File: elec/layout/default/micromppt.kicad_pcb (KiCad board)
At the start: 2 copper layers, 25.9 x 15.3 mm, 16 parts

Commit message: fixed :woozy:
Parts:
- C5: value 1nF ±10% 50V X7R -> 1nF ±20% 50V X7R
- R6: footprint lib:R1206 -> atopile:R1206-bdb864
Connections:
- C1 pad 1: hv-1 -> hv
- C3 pad 1: hv -> hv-1
- R1 pad 1: hv -> hv-1
- R2 pad 1: p3 -> net
- R3 pad 1: hv-1 -> hv
- R5 pad 2: hv -> hv-1
- R6 pad 2: hv -> hv-1
- U2 pad 1: net -> VR2-net
- U2 pad 3: p3 -> net
- U3 pad 1: hv-1 -> hv
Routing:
- net hv-1: track 8.72 -> 13.9 mm, vias 1 -> 3
- net hv: track 13.9 -> 8.72 mm, vias 3 -> 1
- net p3: track 2.22 -> 0.00 mm
- net net: track 0.00 -> 2.22 mm

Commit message: fixed
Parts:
- added U5: , lib:SOD-80_L3.5-W1.5-RD, F.Cu at (50.0, -5.00)
- added U6: 10kΩ ±1% 62.5mW, atopile:R0402-56259e, F.Cu at (10.0, -5.00)
- U2: footprint lib:RES-ADJ-SMD_3224W -> lib:SOT-23_L2.9-W1.3-P1.90-LS2.4-BR
- moved U2 59.4 mm to (80.0, -5.00)
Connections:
- net cathode renamed VOUT
- C1 pad 1: hv -> S
- C3 pad 1: hv-1 -> hv
- R1 pad 1: hv-1 -> hv
- R2 pad 1: net -> VCTRL
- R3 pad 1: hv -> S
- R5 pad 2: hv-1 -> hv
- R6 pad 2: hv-1 -> hv
- U2 pad 1: VR2-net -> G
- U2 pad 2: VCTRL -> S
- U2 pad 3: net -> D
- U3 pad 1: hv -> S
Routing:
- net (no net): track 0.00 -> 21.7 mm, vias 0 -> 3
- net hv-1: track 13.9 -> 0.00 mm, vias 3 -> 0
- net VCTRL: track 13.0 -> 0.00 mm, vias 2 -> 0
- net hv: track 8.72 -> 13.9 mm, vias 1 -> 3
- added copper zone on F.Cu, net (none)
- removed copper zone on F.Cu, net hv-1

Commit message: Micromppt V3 (fr this time)
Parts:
- removed C1: 10µF ±10% 10V X5R, atopile:C0603-bd72f6
- added D1: , lib:SOD-323F_L1.7-W1.3-LS2.5-R-RD, F.Cu at (67.7, 51.9)
- added U7: , lib:CONN-SMD_2P-P2.50_DEALON_XH-2PS, F.Cu at (86.8, 56.3)
- added U8: , lib:CONN-SMD_2P-P2.50_DEALON_XH-2PS, F.Cu at (74.8, 56.3)
- U5: value (none) -> 10µF ±10% 10V X5R; footprint lib:SOD-80_L3.5-W1.5-RD -> atopile:C0603-bd72f6
- moved U6 78.5 mm to (67.6, 48.4), turned to 90 degrees
- moved U2 57.6 mm to (70.7, 51.8), turned to 180 degrees
- moved U5 52.9 mm to (67.6, 44.9), turned to -90 degrees
- moved R2 4.85 mm to (79.0, 52.2), turned to 180 degrees
- moved R3 3.49 mm to (77.0, 44.3)
- moved C3 3.09 mm to (86.5, 50.0), turned to 0 degrees
- moved U3 1.05 mm to (72.0, 46.7)
- moved C4 0.76 mm to (86.7, 44.1)
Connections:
- net S renamed C
- U2 pad 1: G -> A
- U4 pad 1: gnd -> (no net)
- U4 pad 2: gnd -> (no net)
- U4 pad 3: gnd -> (no net)
- U5 pad 2: G -> gnd
- U6 pad 1: G -> A
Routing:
- net C: track 0.00 -> 21.8 mm
- net (no net): track 21.7 -> 0.00 mm, vias 3 -> 0
- net VCTRL: track 0.00 -> 11.5 mm, vias 0 -> 2
- net hv: track 13.9 -> 20.4 mm, vias 3 -> 2
- net D: track 0.00 -> 4.27 mm
- net A: track 0.00 -> 3.85 mm
- net VOUT: track 15.4 -> 12.7 mm
- net net: track 2.22 -> 0.00 mm
- net gnd: track 4.64 -> 2.81 mm, vias 23 -> 10
- net XSHUT: track 16.7 -> 15.5 mm
- added copper zone on F.Cu, net C
- removed copper zone on F.Cu, net hv
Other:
- board size 25.9 x 15.3 mm -> 25.9 x 17.7 mm

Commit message: Micromppt V3 (fr this time) x2
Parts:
- moved R2 0.53 mm to (79.5, 52.5)
- moved D1 0.50 mm to (67.4, 52.3)
- moved U8 0.40 mm to (74.5, 56.3)
- moved U2 0.35 mm to (70.3, 51.9)
- moved R1 0.26 mm to (82.9, 52.5)
- moved U7 0.11 mm to (86.8, 56.3)
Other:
- board size 25.9 x 17.7 mm -> 25.7 x 17.5 mm

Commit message: Micromppt V3 added githash
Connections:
- net VOUT renamed cathode
- U4 pad 1: (no net) -> gnd
- U4 pad 2: (no net) -> gnd
- U4 pad 3: (no net) -> gnd
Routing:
- net gnd: track 2.81 -> 6.24 mm, vias 10 -> 16
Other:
- board text added: "+"
- board text added: "BAT"
- board text added: "PV"
- board text added: "{{GITHASH}}"

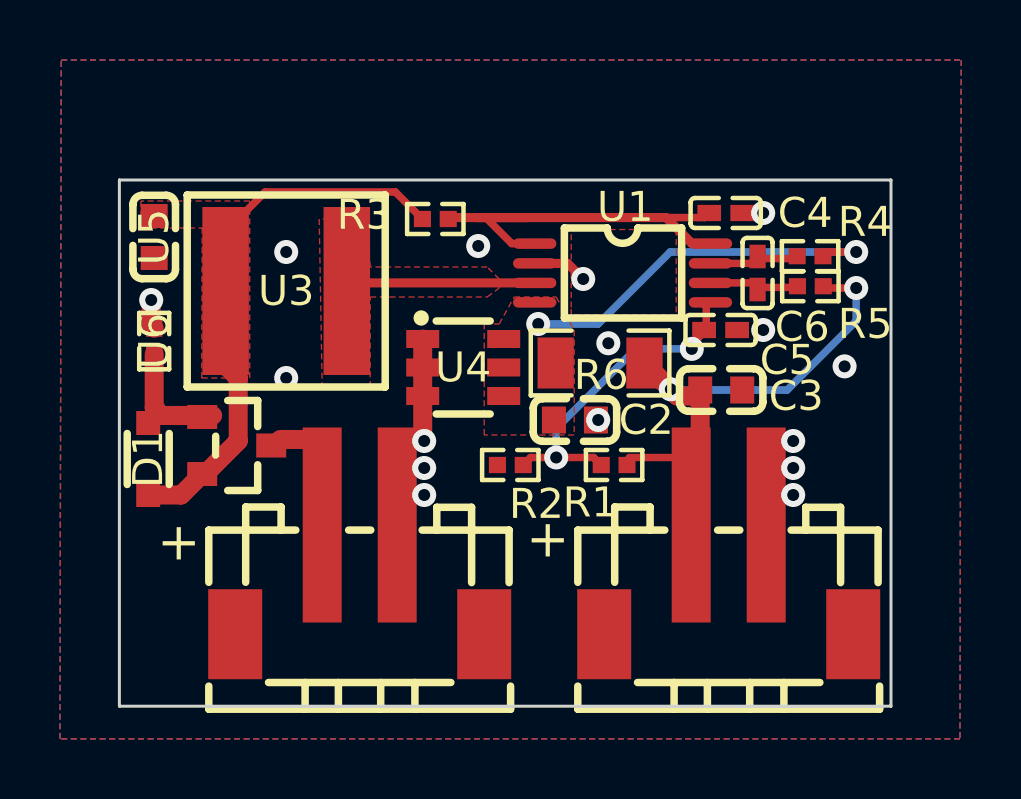
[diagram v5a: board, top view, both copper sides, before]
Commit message: new connector
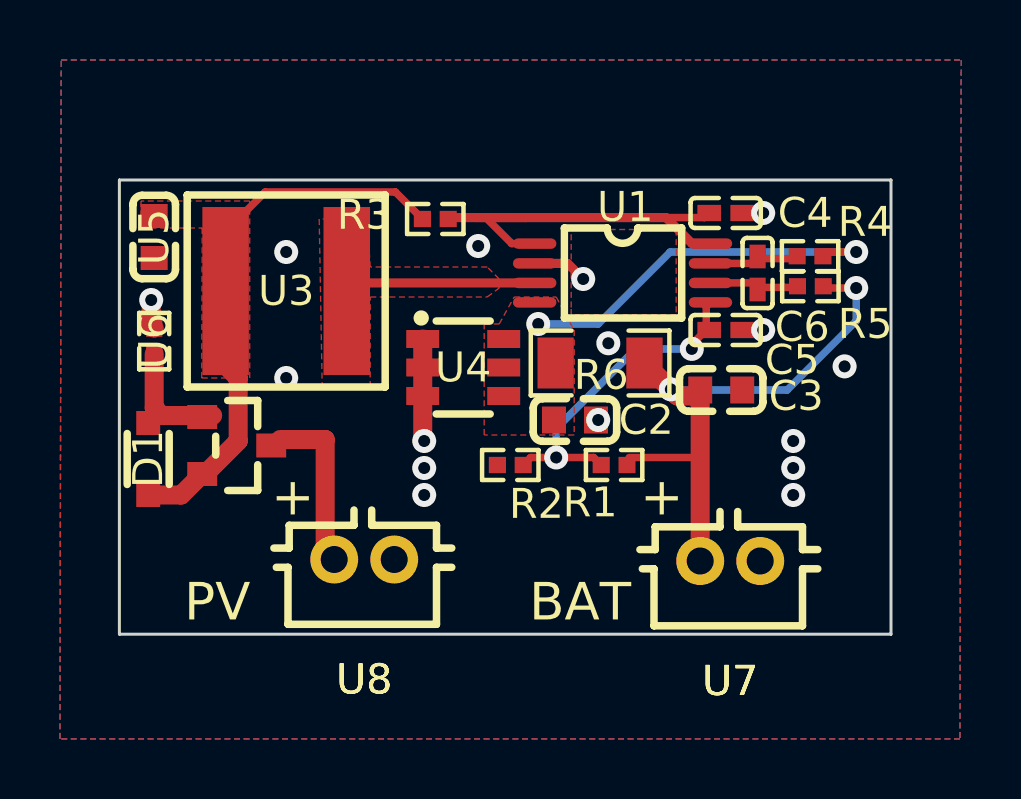
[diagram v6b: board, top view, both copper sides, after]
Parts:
- U7, U8: footprint lib:CONN-SMD_2P-P2.50_DEALON_XH-2PS -> lib:CONN-TH_B2B-PH-K-S
- moved U8 0.69 mm to (74.6, 55.6), turned to 180 degrees
- moved U7 0.62 mm to (86.8, 55.7), turned to 180 degrees
- moved C5 0.17 mm to (86.7, 48.0)
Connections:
- net cathode renamed VOUT
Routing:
- net D: track 4.25 -> 5.62 mm
- net hv: track 20.4 -> 19.4 mm
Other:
- board size 25.7 x 17.5 mm -> 25.7 x 15.1 mm

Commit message: micromppt V3
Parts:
- C2: value 4.7µF ±10% 10V X5R -> 4.7µF ±10% 16V X5R
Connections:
- net VOUT renamed cathode

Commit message: built with ato V3!
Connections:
- net A renamed G
- net C renamed S
- net cathode renamed VOUT
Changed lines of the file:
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@@
     (net 3 "ICTRL_PLUS")
     (net 4 "LX")
-    (net 5 "cathode")
+    (net 5 "VOUT")
     (net 6 "VCTRL")
-    (net 7 "A")
-    (net 8 "C")
+    (net 7 "G")
+    (net 8 "S")
     (net 9 "hv")
     (net 10 "gnd")
@@
             (size 1.1 0.6)
             (layers "F.Cu" "F.Mask" "F.Paste")
-            (net 5 "cathode")
+            (net 5 "VOUT")
             (pintype "stereo")
         )
@@
             (size 1.1 0.6)
             (layers "F.Cu" "F.Mask" "F.Paste")
-            (net 5 "cathode")
+            (net 5 "VOUT")
             (pintype "stereo")
         )
@@
             (size 1.1 0.6)
             (layers "F.Cu" "F.Mask" "F.Paste")
-            (net 5 "cathode")
+            (net 5 "VOUT")
             (pintype "stereo")
         )
@@
             (size 0.8 0.9)
             (layers "F.Cu" "F.Mask" "F.Paste")
-            (net 8 "C")
+            (net 8 "S")
         )
         (pad "2" smd rect
@@
             (size 0.57 0.54)
             (layers "F.Cu" "F.Mask" "F.Paste")
-            (net 7 "A")
+            (net 7 "G")
         )
         (pad "2" smd rect
@@
             (size 0.35 1.45)
             (layers "F.Cu" "F.Mask" "F.Paste")
-            (net 5 "cathode")
+            (net 5 "VOUT")
             (pintype "stereo")
         )
@@
             (size 0.8 0.8)
             (layers "F.Cu" "F.Mask" "F.Paste")
-            (net 8 "C")
+            (net 8 "S")
         )
         (pad "2" smd rect
@@
             (size 0.8 0.8)
             (layers "F.Cu" "F.Mask" "F.Paste")
-            (net 7 "A")
+            (net 7 "G")
         )
         (embedded_fonts no)
@@
             (size 0.57 0.54)
             (layers "F.Cu" "F.Mask" "F.Paste")
-            (net 5 "cathode")
+            (net 5 "VOUT")
         )
         (embedded_fonts no)
@@
             (size 1.55 5.6)
             (layers "F.Cu" "F.Mask" "F.Paste")
-            (net 8 "C")
+            (net 8 "S")
             (pintype "stereo")
         )
@@
             (size 0.8 0.9)
             (layers "F.Cu" "F.Mask" "F.Paste")
-            (net 5 "cathode")
+            (net 5 "VOUT")
         )
         (pad "2" smd rect
@@
             (size 1.21 1.7)
             (layers "F.Cu" "F.Mask" "F.Paste")
-            (net 5 "cathode")
+            (net 5 "VOUT")
         )
         (pad "2" smd rect
@@
             (size 0.57 0.54)
             (layers "F.Cu" "F.Mask" "F.Paste")
-            (net 8 "C")
+            (net 8 "S")
         )
         (pad "2" smd rect
@@
             (size 1 0.8)
             (layers "F.Cu" "F.Mask" "F.Paste")
-            (net 7 "A")
+            (net 7 "G")
         )
         (pad "2" smd rect
@@
             (size 1 0.8)
             (layers "F.Cu" "F.Mask" "F.Paste")
-            (net 8 "C")
+            (net 8 "S")
         )
         (pad "3" smd rect
@@
     (zone
         (net 8)
-        (net_name "C")
+        (net_name "S")
         (layers "F.Cu")
         (hatch edge 0.5)
@@
     (zone
         (net 5)
-        (net_name "cathode")
+        (net_name "VOUT")
         (layers "F.Cu")
         (hatch edge 0.5)
